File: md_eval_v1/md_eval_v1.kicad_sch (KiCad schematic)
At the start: 39 parts, among them J1 Conn_01x02, J10 Conn_01x03, J11 Conn_01x02, J12 Conn_01x02, J14 Conn_01x01, J15 Conn_01x01, J16 Conn_01x01, J17 Conn_01x01, J18 Conn_01x01, J19 Conn_01x01, J2 Conn_01x02, J20 Conn_01x01, J21 Conn_01x01, J22 Conn_01x01, J3 Conn_01x02, J4 Conn_01x02, J5 Conn_01x02, J6 Conn_01x02, J7 Conn_01x02, J8 Conn_01x02, U1 MCT8316Z0TRGFR

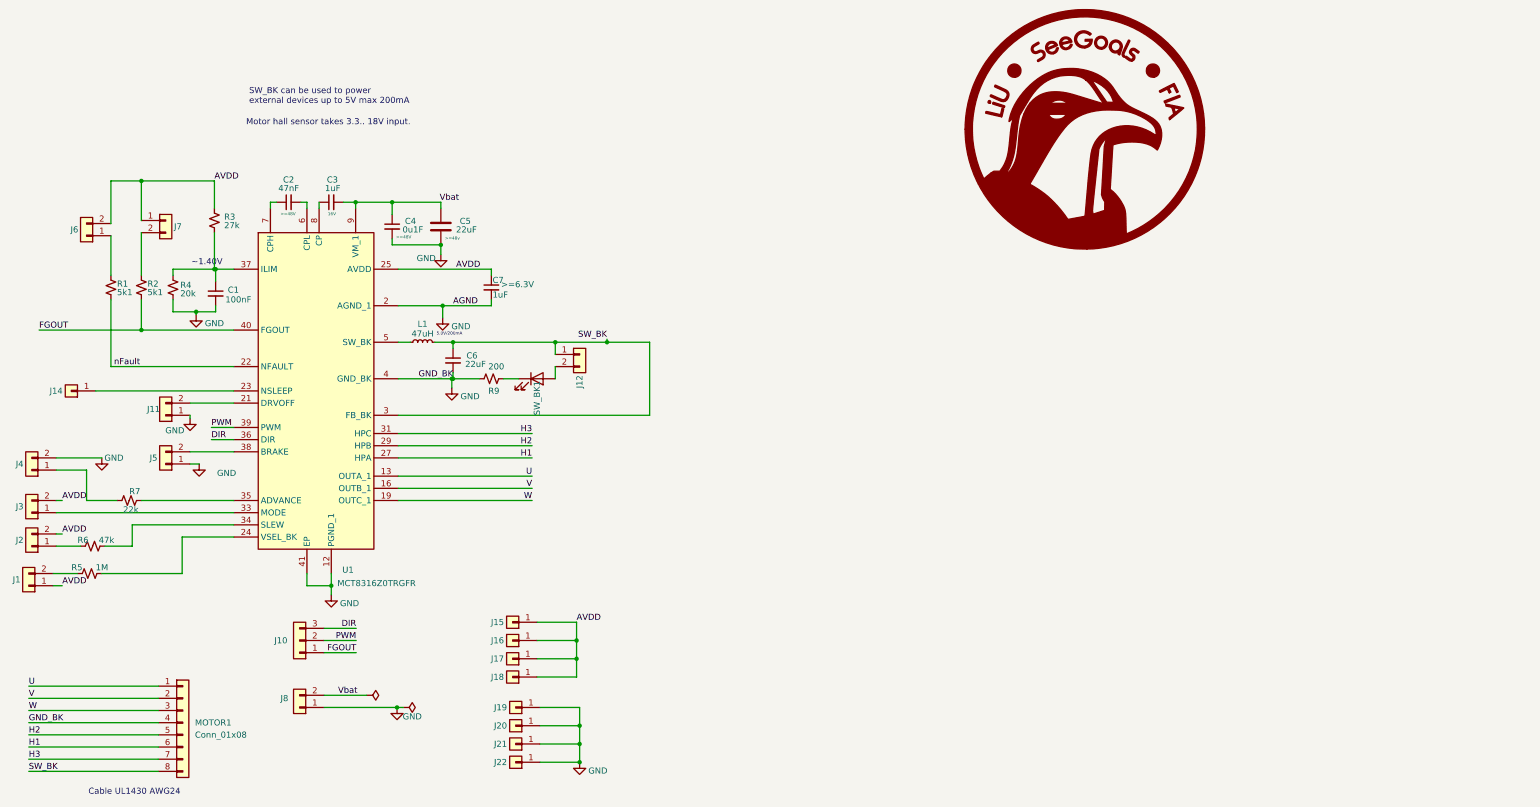
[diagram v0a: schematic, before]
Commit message: Files enhanced
Added uniform titleblocks and 3D renders for easier view.
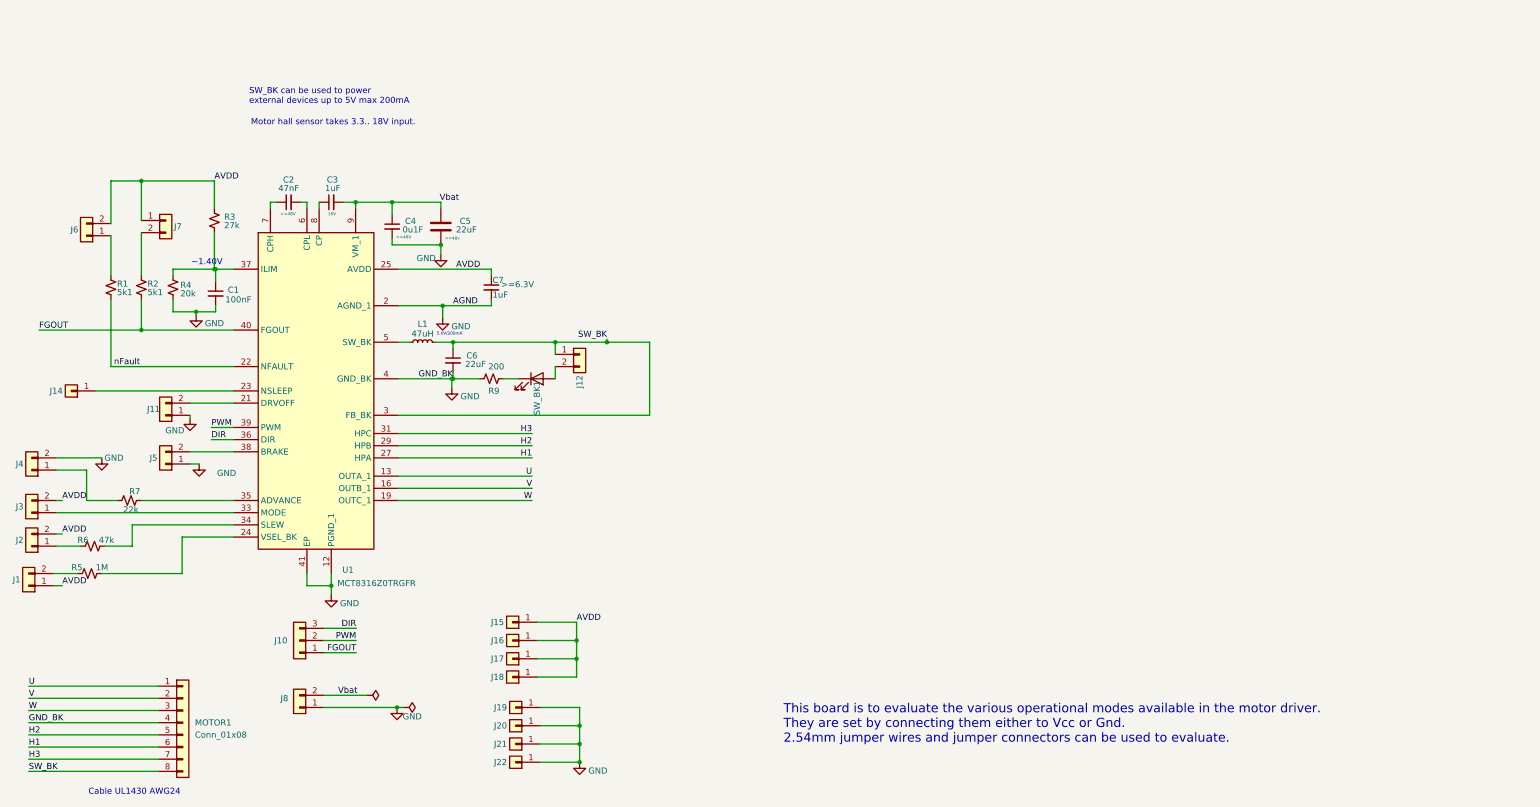
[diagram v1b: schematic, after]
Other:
- note added: "This board is to evaluate the various operational modes available in the motor driver. They are set by connecting them either to Vcc or Gnd. 2.54mm jumper wires and jumper connectors can be used to evaluate."
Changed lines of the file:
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@@
 	(title_block
 		(title "Motor driver evaluation board")
-		(date "2025-07-24")
-		(comment 1 "Designed by Aditya Dharamshi")
+		(date "24-07-2025")
+		(rev "1")
+	)
+	(text "This board is to evaluate the various operational modes available in the motor driver.\nThey are set by connecting them either to Vcc or Gnd.\n2.54mm jumper wires and jumper connectors can be used to evaluate."
+		(exclude_from_sim no)
+		(at 195.58 170.815 0)
+		(effects
+			(font
+				(size 1.905 1.905)
+			)
+			(justify left bottom)
+		)
 	)
 	(text "5.0V/200mA"
@@
 	(text "Motor hall sensor takes 3.3.. 18V input."
 		(exclude_from_sim no)
-		(at 83.439 41.91 0)
+		(at 84.455 41.91 0)
 		(effects
 			(font
@@
 	)
 	(image
-		(at 220.345 125.095)
+		(at 243.84 90.805)
 		(scale 0.386103)
 		(data "iVBORw0KGgoAAAANSUhEUgAAArcAAAJpCAIAAAA4y41/AAAAA3NCSVQICAjb4U/gAAAACXBIWXMA"
@@
 	)
 	(image
-		(at 213.106 71.12)
+		(at 242.316 40.64)
 		(scale 0.205596)
 		(data "iVBORw0KGgoAAAANSUhEUgAAAm4AAAL2CAIAAAB3/41qAAAAA3NCSVQICAjb4U/gAAAACXBIWXMA"
@@
 	)
 	(symbol
-		(lib_id "Logo:LOGO")
-		(at 258.445 42.545 0)
-		(unit 1)
-		(exclude_from_sim no)
-		(in_bom yes)
-		(on_board yes)
-		(dnp no)
-		(fields_autoplaced yes)
-		(property "Reference" "#G1"
-			(at 258.445 -137.482 0)
-			(effects
-				(font
-					(size 1.27 1.27)
-				)
-				(hide yes)
-			)
-		)
-		(property "Value" "LOGO"
-			(at 258.445 222.572 0)
-			(effects
-				(font
-					(size 1.27 1.27)
-				)
-				(hide yes)
-			)
-		)
-		(property "Footprint" ""
-			(at 258.445 42.545 0)
-			(effects
-				(font
-					(size 1.27 1.27)
-				)
-				(hide yes)
-			)
-		)
-		(property "Datasheet" ""
-			(at 258.445 42.545 0)
-			(effects
-				(font
-					(size 1.27 1.27)
-				)
-				(hide yes)
-			)
-		)
-		(property "Description" ""
-			(at 258.445 42.545 0)
-			(effects
-				(font
-					(size 1.27 1.27)
-				)
-				(hide yes)
-			)
-		)
-		(instances
-			(project "md_eval_v1"
-				(path "/a239882f-20b1-428d-a60f-69846bd56326"
-					(reference "#G1")
-					(unit 1)
-				)
-			)
-		)
-	)
-	(symbol
 		(lib_id "Device:C_Small")
 		(at 134.62 75.565 0)
@@
 	)
 	(embedded_fonts no)
+	(embedded_files
+		(file
+			(name "SeeGoals.kicad_wks")
+			(type worksheet)
+			(data |KLUv/WBWCEUVAKZhaSDwGD3QEeyM1Nkm1gfAFENB192U/Uu5smaFjYXFwbleVGAAXQBiAJ3fHl7X
+				Y9LV3cOctHvfXWn3EChzOV9nEL8kT/9g0GBnlB/qX0ZhnUGDjfPxKoc9hXsBAAgISqaOQxm3y3Pl
+				D3vA0vV898uxxiCDNuesVNLXO4ccnwqAgCAcoTzf9fKoENH+NmmcG61b1B6zWMxqi9MsGh5uk8lE
+				WIRX4H4bnHMVx11j71Wf3EOTyNKfCxW1L7uuk7MWAF3vz3xLP9yla17fU7h33cpq6UurSnFPZ/r9
+				4hJ++Z/GHGu+vQ7KD5SjLCrcJOLIDi+Dt+c30KfUblic9K1mo9wmmogG7Fnz5e8YhzK0alGbn2ED
+				RGvwRT5wd09nzWKdNcLhMCeMuf67XpZc3zUmkbaXYVqsP7OKJZLBcBxPY8GISFgEm8lIqUzYAYFh
+				5G2w+/441P/Tps3vY7NWardYp+6EXu6725hfRBx/CMG7Hxhfr9K3RNqMLRHrJyxGE1rUvkqaQyHp
+				8htq/FX1/C1eoer+wxqUQ9ygWcQgmsVFw3GQjJQxMbMsizNqoPE4ZRwaqlGQNhnGUISIGbtuzyGn
+				lKLOBfFKGKkDMleBRYmd+5lzd8a/EMWXlwELeZPPxs5h2q26xzeF3cWJrdCkNHThwclSRVgc7Dxs
+				MDMBL5YFRtvnhSGIHvsw9DvTX0LDM7kiJLLMgQAug8cycePhfwgg9p0jKCmmgSwuO10DIfREMvJw
+				LLj/XY/Uc30G6agTD3QoENPIaa/cRm4toMWW/gBBiO5x6hcVBV46gAt257j3s/hpM5Qllp35xv/E
+				NrWcdAgCmKGamAagRtgP3ENBfATG+0F8zQAN0JLmhSfpliXkbEcKm+yAvU9vmyZDF97SNzwfcQcZ
+				bgE1BqEK|
+			)
+			(checksum "714487A7A475B68BB3B3E7DC8D393DDF")
+		)
+	)
 )
